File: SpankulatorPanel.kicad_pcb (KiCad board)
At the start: 2 copper layers, 60.4 x 128.4 mm, 33 parts, among them J1 OLED Pins

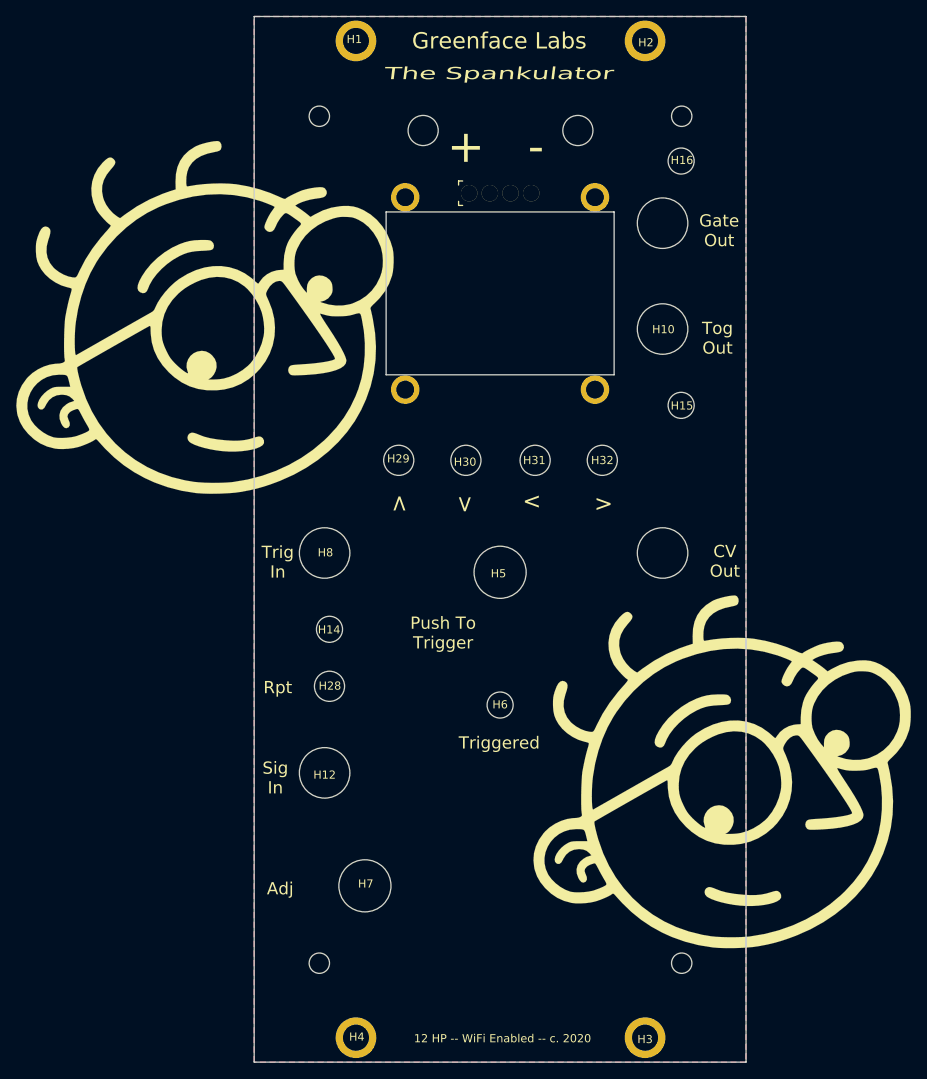
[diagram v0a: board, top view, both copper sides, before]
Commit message: Adds front panel graphics. Removes OLED mounting hardware.
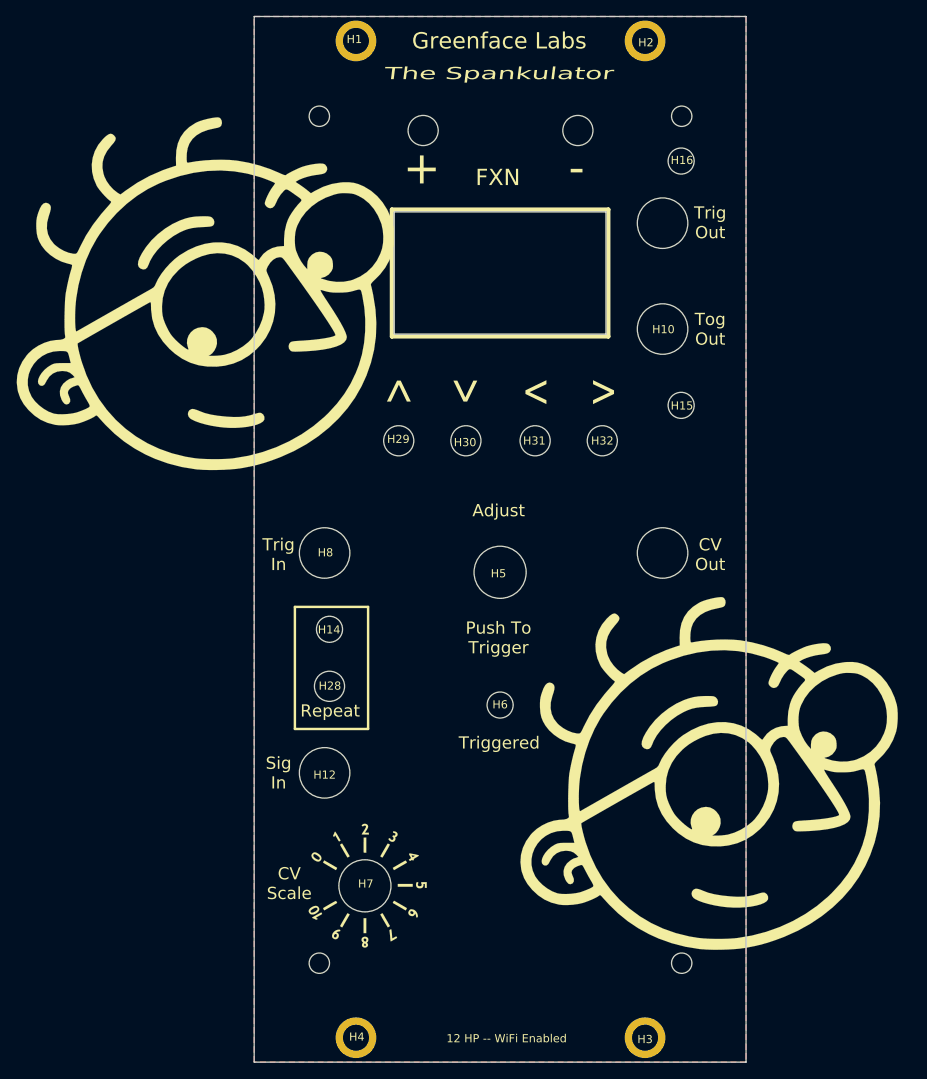
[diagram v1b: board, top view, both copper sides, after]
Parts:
- removed the G*** at (48.8, 78.4)
- removed the G*** at (112.3, 134.2)
- removed H21, H22, H23, H24: MountingHole, MountingHole:MountingHole_2.2mm_M2_ISO7380_Pad
- removed J1: OLED Pins, panel:OLED_Pins
- added G***: LOGO, panel:dial2, F.Cu at (68.9, 146.7)
- added G***: LOGO, panel:face_logo, F.Cu at (110.7, 134.4)
- added G***: LOGO, panel:face_logo, F.Cu at (48.9, 75.5)
- moved H29 2.40 mm to (72.8, 92.1)
- moved H30 2.40 mm to (81.0, 92.1)
- moved H31 2.40 mm to (89.5, 92.1)
- moved H32 2.40 mm to (97.8, 92.1)
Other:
- outline, holes or cut-outs redrawn
- board text added: "12 HP -- WiFi Enabled"
- board text added: "Adjust"
- board text added: "CV Scale"
- board text added: "FXN"
- board text added: "Repeat"
- board text added: "Trig Out"
- board text added: "v2.3"
- board text removed: "12 HP -- WiFi Enabled -- c. 2020"
- board text removed: "Adj"
- board text removed: "Gate Out"
- board text removed: "Rpt"

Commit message: version 3.0
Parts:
- moved G*** 3.91 mm to (65.0, 146.6), turned to 90 degrees
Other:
- board text added: "Greenface Labs "The Spankulator" v3.0"
- board text removed: "v2.3"
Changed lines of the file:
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@@
     (mod_text_size 1 1)
     (mod_text_width 0.15)
-    (pad_size 3.7 3.7)
-    (pad_drill 3.7)
+    (pad_size 6.4 6.4)
+    (pad_drill 6.4)
     (pad_to_mask_clearance 0.051)
     (solder_mask_min_width 0.25)
@@
   )
   (module panel:dial2 (layer F.Cu)
-    (at 68.91 146.72)
-    (fp_text reference G*** (at 0 0) (layer F.SilkS) hide
+    (at 65 146.55 90)
+    (fp_text reference G*** (at 0 0 90) (layer F.SilkS) hide
       (effects (font (size 1.524 1.524) (thickness 0.3)))
     )
-    (fp_text value LOGO (at 0.75 0) (layer F.SilkS) hide
+    (fp_text value LOGO (at -0.1 0 90) (layer F.SilkS) hide
       (effects (font (size 1.524 1.524) (thickness 0.3)))
     )
@@
     (tags "mounting hole 6.4mm no annular m6 din965")
     (attr virtual)
-    (fp_text reference H7 (at 0.1 -0.25) (layer F.SilkS)
+    (fp_text reference H7 (at -3.6 0.25) (layer F.SilkS)
       (effects (font (size 1 1) (thickness 0.15)))
     )
@@
     (fp_circle (center 0 0) (end 5.5 0) (layer Cmts.User) (width 0.15))
     (fp_circle (center 0 0) (end 5.75 0) (layer F.CrtYd) (width 0.05))
-    (pad 1 np_thru_hole circle (at 0 0) (size 6.4 6.4) (drill 6.4) (layers *.Cu *.Mask))
+    (pad "" np_thru_hole circle (at -3.6 0) (size 6.4 6.4) (drill 6.4) (layers *.Cu *.Mask))
   )
   (module MountingHole:MountingHole_3.2mm_M3_DIN965 (layer F.Cu)
@@
     (fp_circle (center 0 0) (end 3.05 0) (layer F.CrtYd) (width 0.05))
     (pad 1 np_thru_hole circle (at 0 0) (size 3.2 3.2) (drill 3.2) (layers *.Cu *.Mask))
+  )
+  (gr_text "Greenface Labs\n\"The Spankulator\"\nv3.0" (at 85.75 161.75) (layer B.SilkS)
+    (effects (font (size 1.5 1.5) (thickness 0.25)) (justify mirror))
   )
   (gr_line (start 60 127.49) (end 60 112.5) (layer F.SilkS) (width 0.3))
@@
     (effects (font (size 1.5 1.5) (thickness 0.3)))
   )
-  (gr_text FXN (at 84.925 59.775) (layer F.SilkS)
-    (effects (font (size 2 2) (thickness 0.3)))
-  )
-  (gr_text v2.3 (at 86.3 45.65) (layer B.SilkS)
-    (effects (font (size 3 3) (thickness 0.3)) (justify mirror))
+  (gr_text FXN (at 84.925 59) (layer F.SilkS)
+    (effects (font (size 3 2.5) (thickness 0.3)))
   )
   (gr_text Triggered (at 85.1 129.2) (layer F.SilkS)
@@
     (effects (font (size 1.5 1.5) (thickness 0.3)))
   )
-  (gr_text "CV \nScale" (at 59.31 146.47) (layer F.SilkS)
+  (gr_text "CV \nScale" (at 76.05 146.31) (layer F.SilkS)
     (effects (font (size 1.5 1.5) (thickness 0.3)))
   )
